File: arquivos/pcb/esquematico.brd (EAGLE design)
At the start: 60 x 50 mm, 14 parts, among them IC1 LM35CZ, IC2 LM35CZ, J1 694108210102, Q1 TIP31, Q2 TIP31

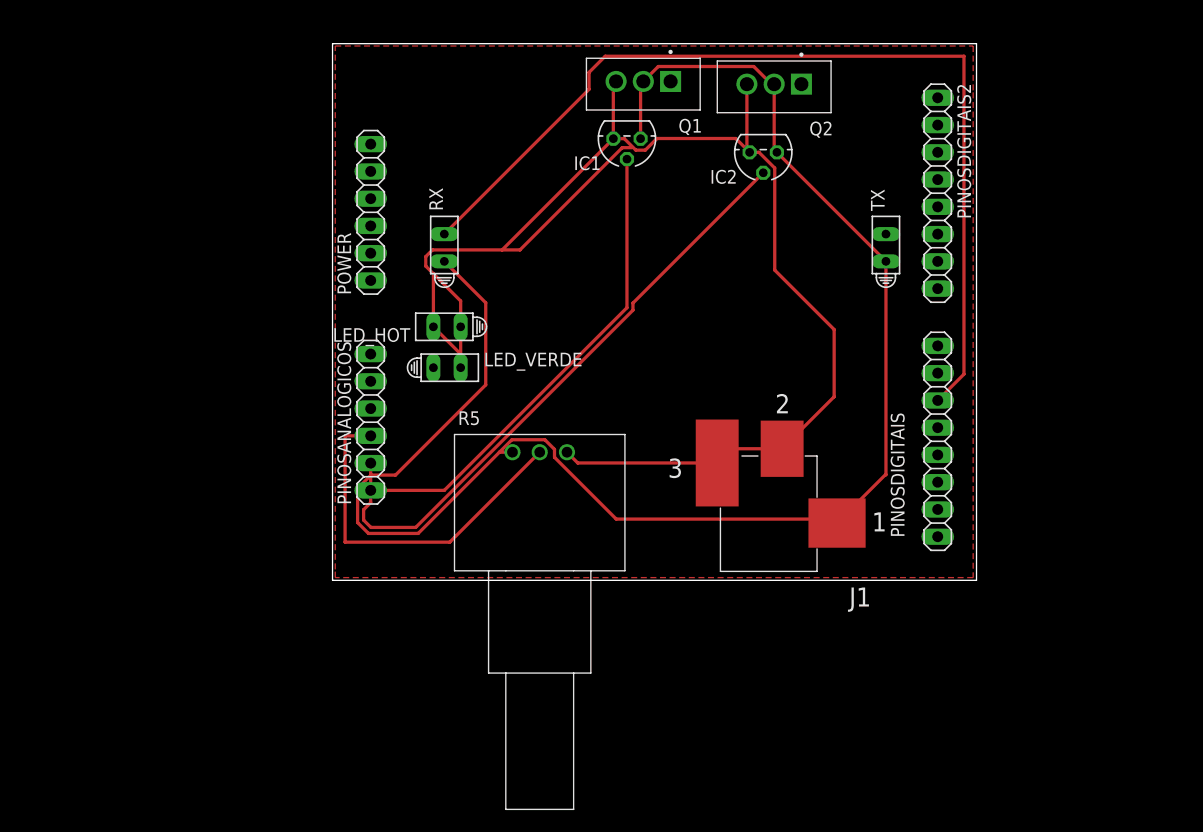
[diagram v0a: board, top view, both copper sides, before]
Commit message: Esquematico atualizado
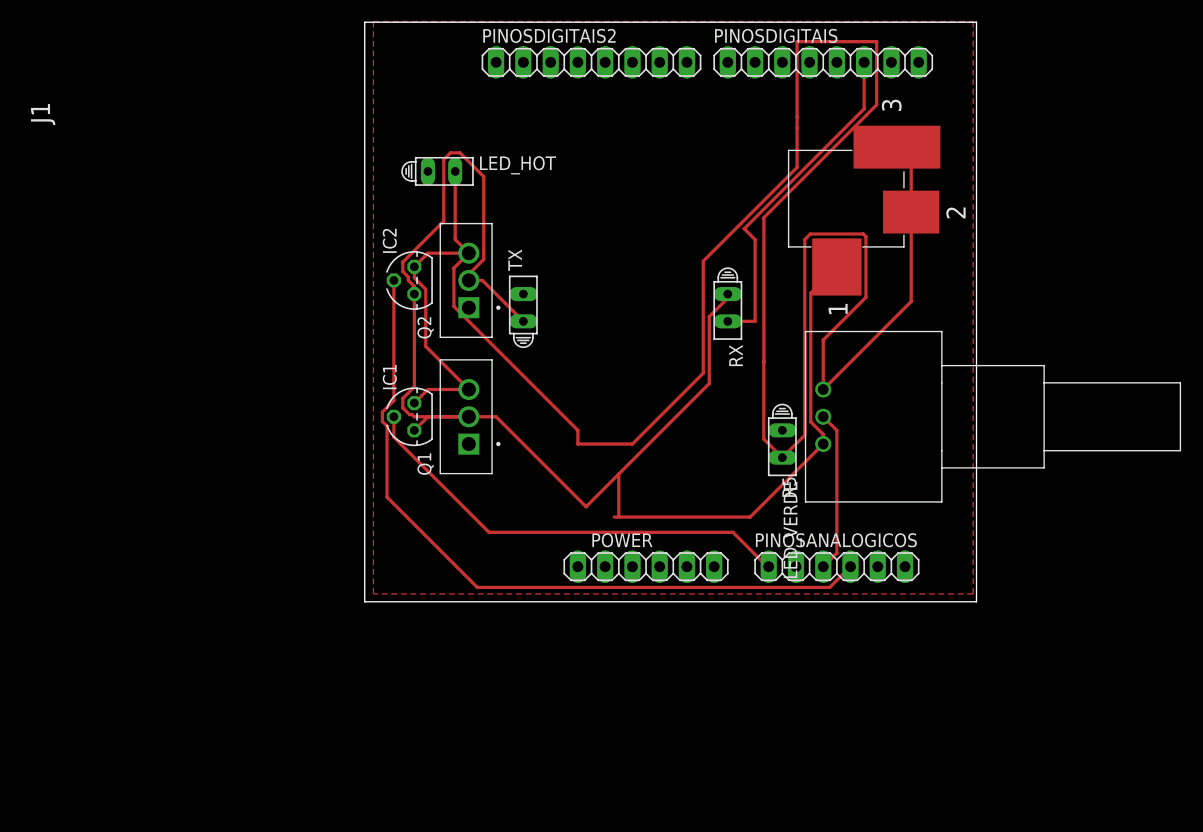
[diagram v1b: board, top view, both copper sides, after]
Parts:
- moved PINOSANALOGICOS 45.5 mm to (47.0, 1.27), turned to 0 degrees
- moved POWER 41.8 mm to (29.2, 1.27), turned to 0 degrees
- moved PINOSDIGITAIS 36.9 mm to (45.7, 48.3), turned to 0 degrees
- moved Q1 35.2 mm to (12.7, 15.2), turned to 90 degrees
- moved IC2 34.6 mm to (7.62, 27.9), turned to 90 degrees
- moved PINOSDIGITAIS2 34.5 mm to (24.1, 48.3), turned to 0 degrees
- moved TX 34.2 mm to (17.8, 25.4)
- moved Q2 33.8 mm to (12.7, 27.9), turned to 90 degrees
- moved IC1 32.6 mm to (7.62, 15.2), turned to 90 degrees
- moved LED_VERDE 32.0 mm to (41.9, 12.7), turned to 270 degrees
- moved J1 30.9 mm to (47.0, 35.6), turned to 90 degrees
- moved RX 27.0 mm to (36.8, 25.4), turned to 270 degrees
- moved R5 26.6 mm to (45.7, 15.2), turned to 90 degrees
- moved LED_HOT 14.5 mm to (10.2, 38.1), turned to 0 degrees
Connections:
- net N$1: now also PINOSANALOGICOS.4; no longer PINOSANALOGICOS.2
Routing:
- net GND: track 140.0 -> 225.8 mm
- net N$9: track 89.3 -> 31.7 mm
- net N$13: track 33.9 -> 15.0 mm
- net N$1: track 57.2 -> 68.3 mm
- net +5V: track 152.5 -> 143.5 mm
- net N$14: track 44.8 -> 41.8 mm
- added copper zone on layer 1, net TERRA
- removed copper zone on layer 1, net PLANO_DE_TERRA
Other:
- board size 60 x 50 mm -> 57 x 54 mm
